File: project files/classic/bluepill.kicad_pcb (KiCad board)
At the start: 2 copper layers, 53.3 x 22.9 mm, 39 parts, among them J1 USB_B_Micro, J2 Boot, J3 Left Row, J4 SWD, J5 Right Row, SW1 Reset, U1 RT8183-33, U2 STM32F103C8Tx, Y1 8MHz, Y2 32768Hz

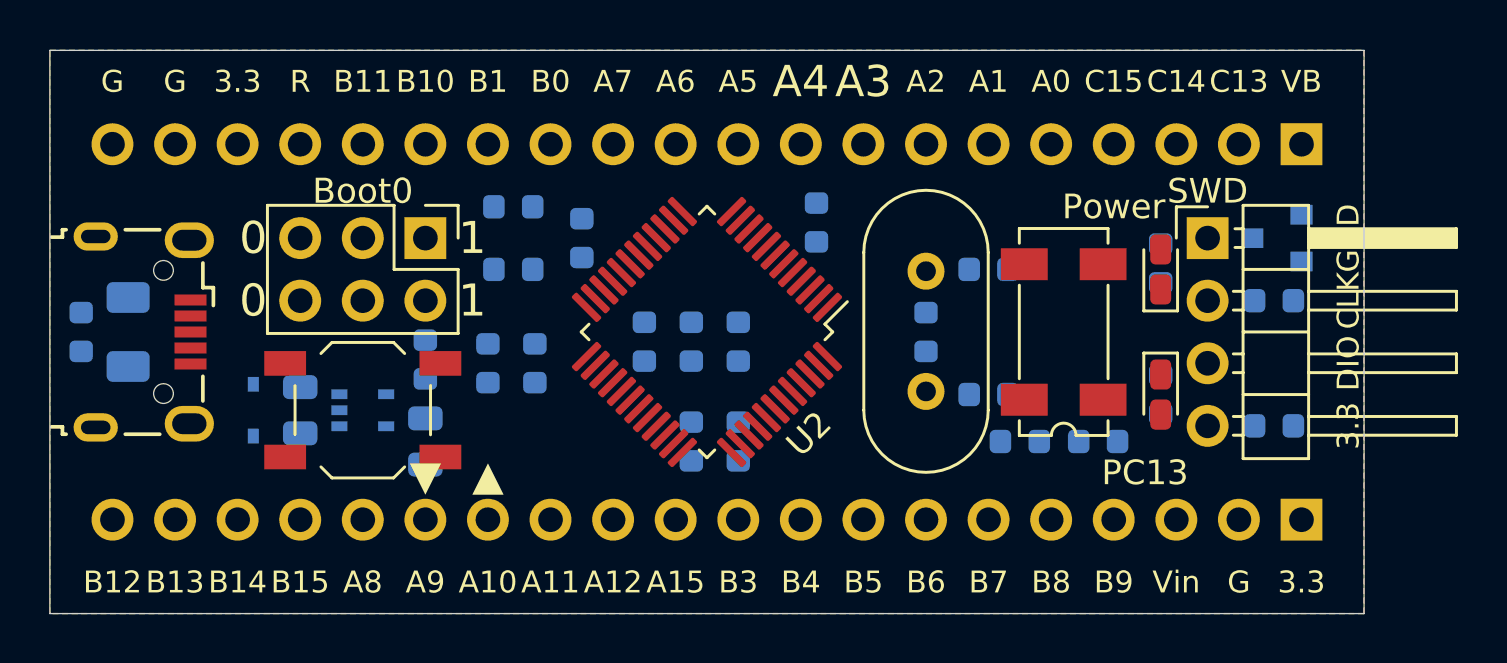
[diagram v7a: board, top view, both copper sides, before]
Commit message: Added Readme.md and minor changes to classic layout
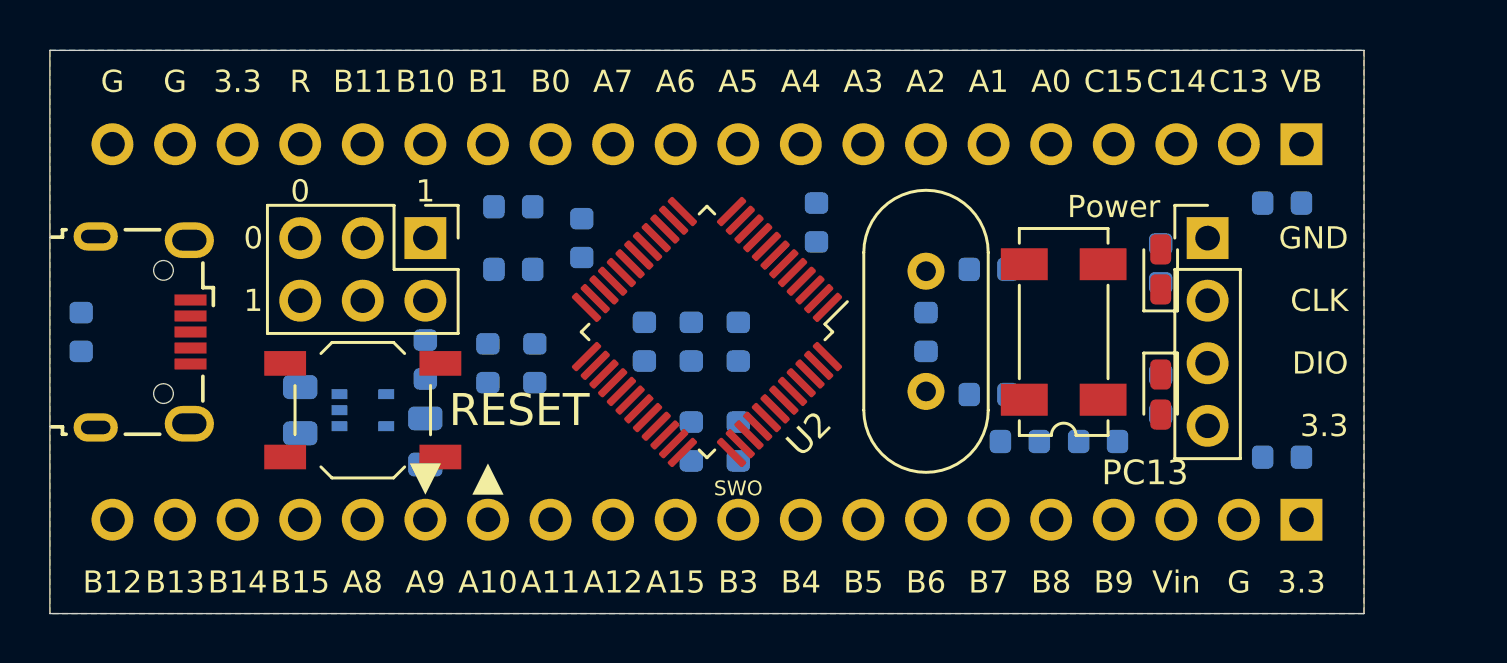
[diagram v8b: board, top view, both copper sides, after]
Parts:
- removed D1: SD103AWS, Diode_SMD:D_SOD-323
- removed D4: BAT54C, Package_TO_SOT_SMD:SOT-23
- removed F1: 500mA, Fuse:Fuse_1206_3216Metric
- J4: footprint Connector_PinHeader_2.54mm:PinHeader_1x04_P2.54mm_Horizontal -> Connector_PinHeader_2.54mm:PinHeader_1x04_P2.54mm_Vertical
- moved C10 3.98 mm to (156.7, 120.5), turned to 180 degrees
- moved C15 1.31 mm to (156.7, 130.8), turned to 180 degrees
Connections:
- C10 pad 1: Vbat_protected -> +BATT
- C2 pad 1: Net-(C2-Pad1) -> +5V
- J1 pad 1: VBUS -> +5V
- U2 pad 1: Vbat_protected -> +BATT
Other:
- board text added: "RESET"
- board text added: "SWO"
- board text removed: "Boot0"
